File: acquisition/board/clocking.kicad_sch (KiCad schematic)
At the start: 58 parts, among them U11 LMK04806, U12 SIT9002AC-232N33EO100.00000, U14 74AVCH1T45, U15 74AVCH1T45, U16 74AVCH1T45, U17 74AVCH1T45, U19 74AVCH1T45, U20 74AVCH1T45

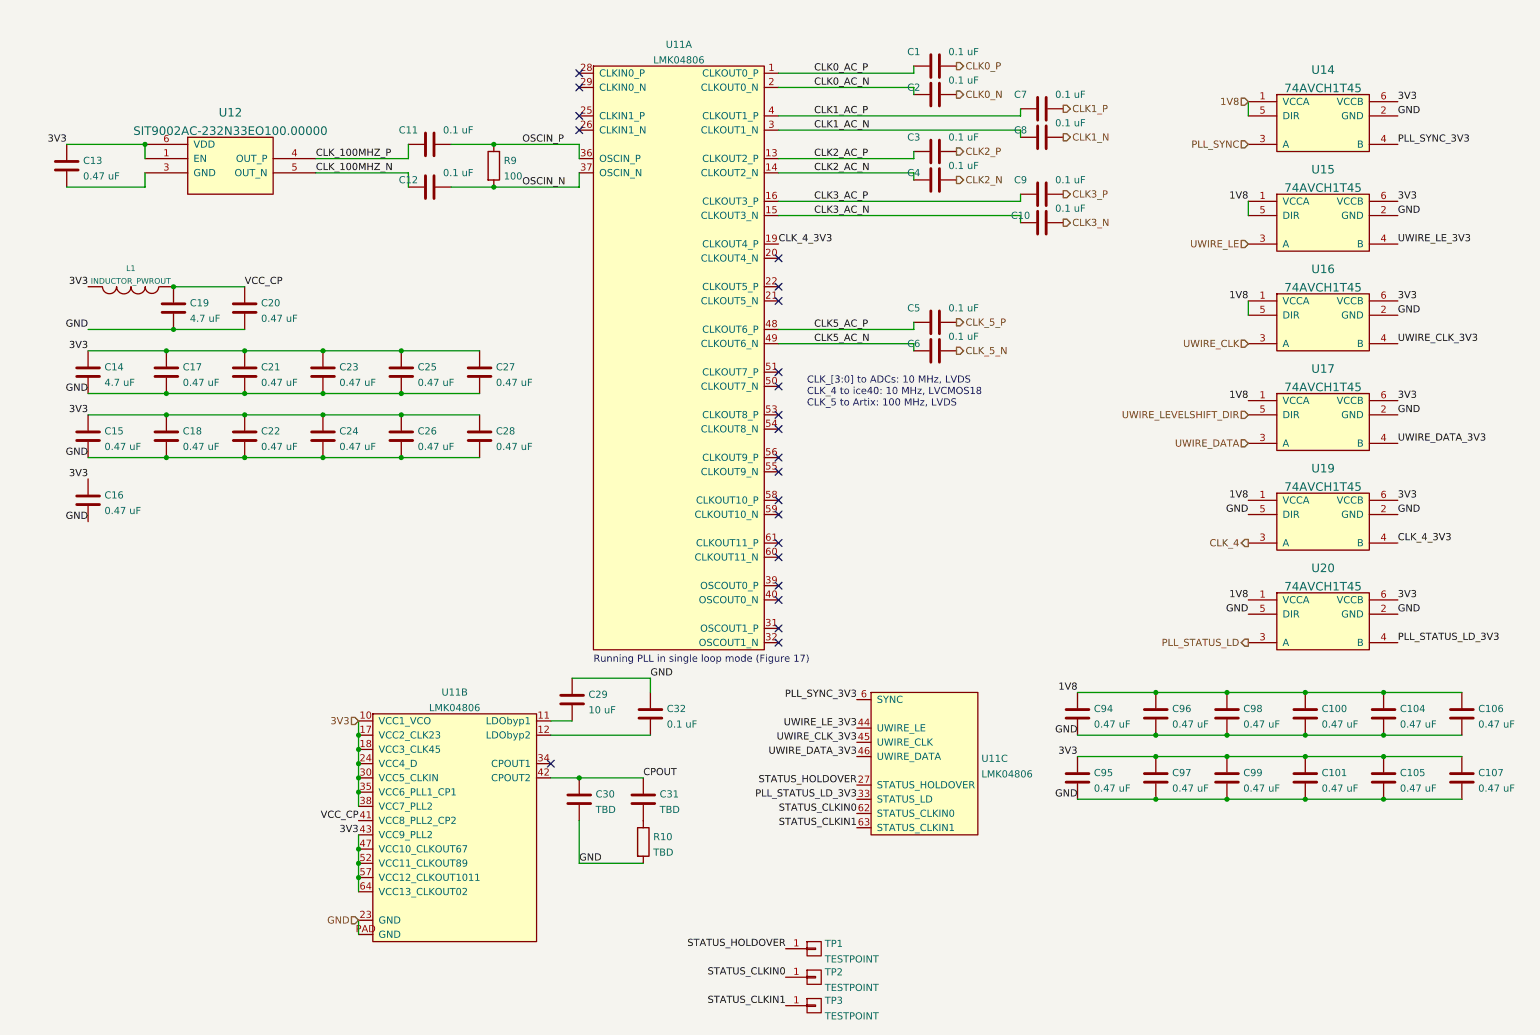
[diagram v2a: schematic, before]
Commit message: Lots of progress on power supply design, added a bunch of test points, etc
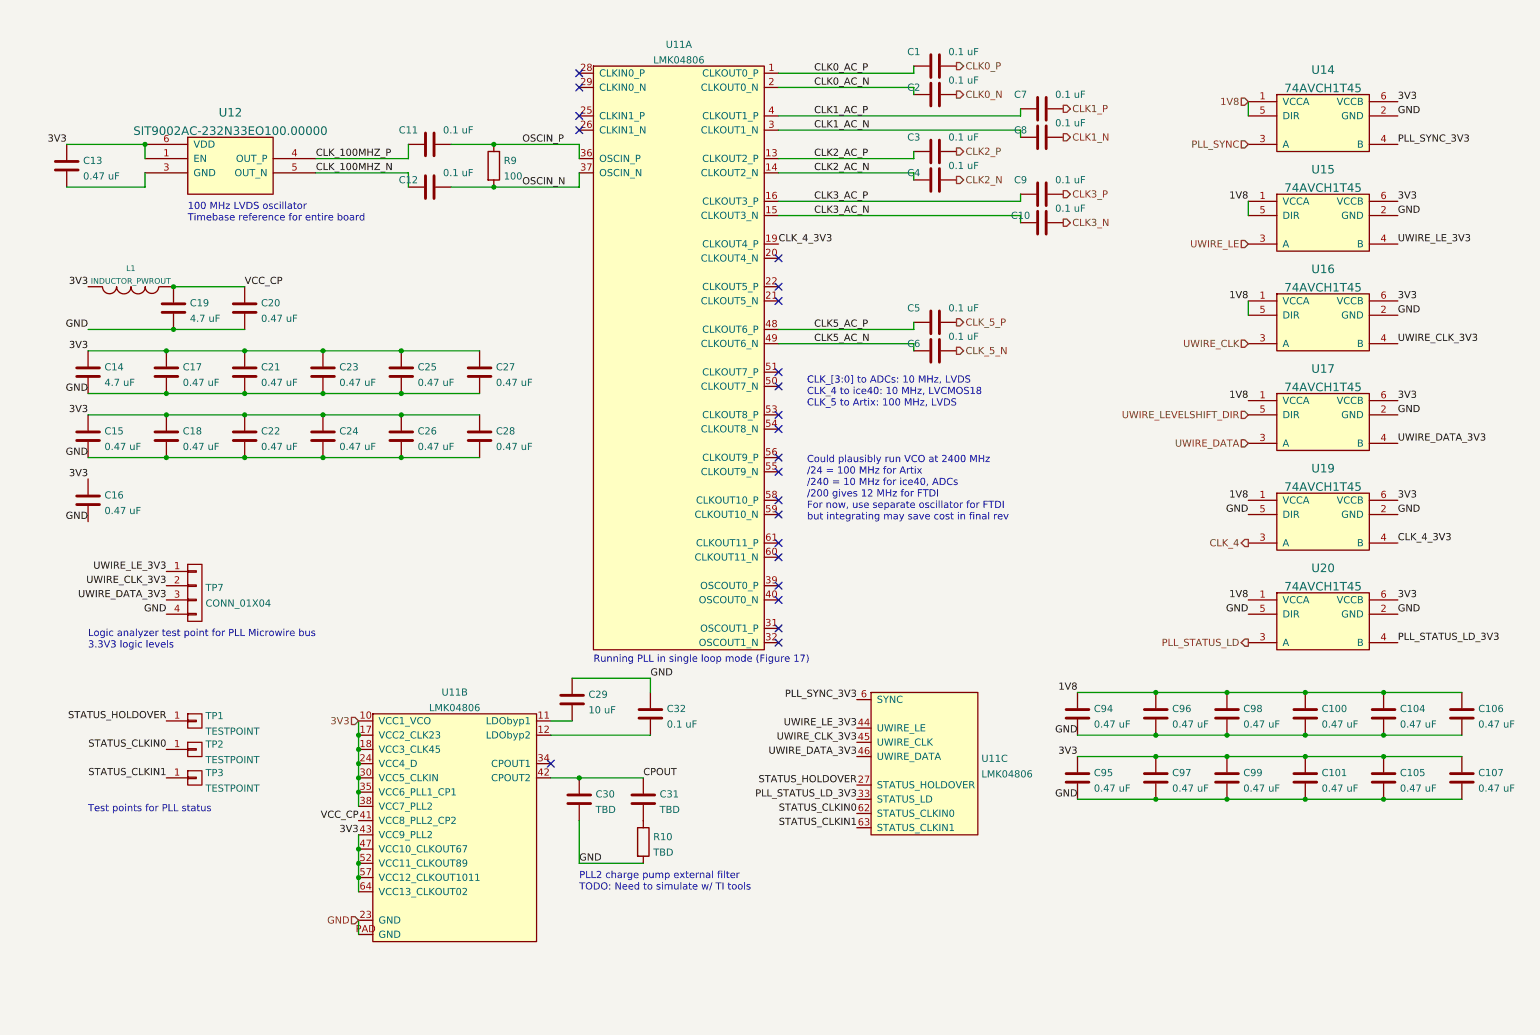
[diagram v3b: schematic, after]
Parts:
- added TP7: CONN_01X04, symbol conn:CONN_01X04
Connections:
- net GND: now also TP7.4 (P4)
- net UWIRE_CLK_3V3: now also TP7.2 (P2)
- net UWIRE_DATA_3V3: now also TP7.3 (P3)
- net UWIRE_LE_3V3: now also TP7.1 (P1)
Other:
- note added: "100 MHz LVDS oscillator Timebase reference for entire board"
- note added: "Could plausibly run VCO at 2400 MHz /24 = 100 MHz for Artix /240 = 10 MHz for ice40, ADCs /200 gives 12 MHz for FTDI For now, use separate oscillator for FTDI but integrating may save cost in final rev"
- note added: "Logic analyzer test point for PLL Microwire bus 3.3V3 logic levels"
- note added: "PLL2 charge pump external filter TODO: Need to simulate w/ TI tools"
- note added: "Test points for PLL status"
- moved on the sheet: TP1, TP2, TP3
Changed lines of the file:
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@@
   (title_block
     (title "Digitizer board")
-    (date "2022-07-04")
+    (date "2022-07-05")
     (rev "0.1")
     (company "A. Zonenberg")
@@
     (stroke (width 0) (type default) (color 0 0 0 0))
   )
+  (text "100 MHz LVDS oscillator\nTimebase reference for entire board"
+    (at 43.18 52.07 0)
+    (effects (font (size 1.27 1.27)) (justify left bottom))
+  )
+  (text "Test points for PLL status" (at 25.4 157.48 0)
+    (effects (font (size 1.27 1.27)) (justify left bottom))
+  )
   (text "CLK_[3:0] to ADCs: 10 MHz, LVDS\nCLK_4 to ice40: 10 MHz, LVCMOS18\nCLK_5 to Artix: 100 MHz, LVDS"
     (at 153.67 85.09 0)
@@
     (effects (font (size 1.27 1.27)) (justify left bottom))
   )
+  (text "Could plausibly run VCO at 2400 MHz\n/24 = 100 MHz for Artix\n/240 = 10 MHz for ice40, ADCs\n/200 gives 12 MHz for FTDI\nFor now, use separate oscillator for FTDI\nbut integrating may save cost in final rev"
+    (at 153.67 105.41 0)
+    (effects (font (size 1.27 1.27)) (justify left bottom))
+  )
+  (text "Logic analyzer test point for PLL Microwire bus\n3.3V3 logic levels"
+    (at 25.4 128.27 0)
+    (effects (font (size 1.27 1.27)) (justify left bottom))
+  )
+  (text "PLL2 charge pump external filter\nTODO: Need to simulate w/ TI tools"
+    (at 113.03 171.45 0)
+    (effects (font (size 1.27 1.27)) (justify left bottom))
+  )
   (label "CLK_4_3V3" (at 259.08 109.22 0)
     (effects (font (size 1.27 1.27)) (justify left bottom))
@@
     (effects (font (size 1.27 1.27)) (justify left bottom))
   )
+  (label "UWIRE_DATA_3V3" (at 39.37 119.38 180)
+    (effects (font (size 1.27 1.27)) (justify right bottom))
+  )
   (label "GND" (at 201.93 143.51 180)
     (effects (font (size 1.27 1.27)) (justify right bottom))
@@
     (effects (font (size 1.27 1.27)) (justify right bottom))
   )
+  (label "UWIRE_LE_3V3" (at 39.37 114.3 180)
+    (effects (font (size 1.27 1.27)) (justify right bottom))
+  )
   (label "UWIRE_DATA_3V3" (at 259.08 91.44 0)
     (effects (font (size 1.27 1.27)) (justify left bottom))
@@
     (effects (font (size 1.27 1.27)) (justify right bottom))
   )
-  (label "STATUS_CLKIN0" (at 149.86 186.69 180)
+  (label "STATUS_CLKIN0" (at 39.37 146.05 180)
     (effects (font (size 1.27 1.27)) (justify right bottom))
   )
@@
     (effects (font (size 1.27 1.27)) (justify left bottom))
   )
+  (label "UWIRE_CLK_3V3" (at 39.37 116.84 180)
+    (effects (font (size 1.27 1.27)) (justify right bottom))
+  )
   (label "UWIRE_CLK_3V3" (at 259.08 73.66 0)
     (effects (font (size 1.27 1.27)) (justify left bottom))
@@
     (effects (font (size 1.27 1.27)) (justify left bottom))
   )
-  (label "STATUS_CLKIN1" (at 149.86 191.77 180)
+  (label "STATUS_CLKIN1" (at 39.37 151.13 180)
     (effects (font (size 1.27 1.27)) (justify right bottom))
   )
@@
     (effects (font (size 1.27 1.27)) (justify left bottom))
   )
-  (label "STATUS_HOLDOVER" (at 149.86 181.61 180)
+  (label "STATUS_HOLDOVER" (at 39.37 140.97 180)
     (effects (font (size 1.27 1.27)) (justify right bottom))
   )
@@
   )
   (label "3V3" (at 25.4 63.5 180)
+    (effects (font (size 1.27 1.27)) (justify right bottom))
+  )
+  (label "GND" (at 39.37 121.92 180)
     (effects (font (size 1.27 1.27)) (justify right bottom))
   )
@@
     (pin "1")
     (pin "2")
+  )
+  (symbol (lib_id "conn:CONN_01X04") (at 44.45 118.11 0) (unit 1)
+    (in_bom yes) (on_board yes) (fields_autoplaced)
+    (property "Reference" "TP7" (id 0) (at 46.355 117.2015 0)
+      (effects (font (size 1.27 1.27)) (justify left))
+    )
+    (property "Value" "CONN_01X04" (id 1) (at 46.355 119.9766 0)
+      (effects (font (size 1.27 1.27)) (justify left))
+    )
+    (property "Footprint" "" (id 2) (at 44.45 118.11 0)
+      (effects (font (size 1.27 1.27)) hide)
+    )
+    (property "Datasheet" "" (id 3) (at 44.45 118.11 0)
+      (effects (font (size 1.27 1.27)) hide)
+    )
+    (pin "1")
+    (pin "2")
+    (pin "3")
+    (pin "4")
   )
   (symbol (lib_id "device:C") (at 53.34 90.17 0) (mirror y) (unit 1)
@@
     (pin "6")
   )
-  (symbol (lib_id "conn:CONN_01X01") (at 154.94 191.77 0) (unit 1)
-    (in_bom yes) (on_board yes) (fields_autoplaced)
-    (property "Reference" "TP3" (id 0) (at 156.845 190.8615 0)
-      (effects (font (size 1.27 1.27)) (justify left))
-    )
-    (property "Value" "TESTPOINT" (id 1) (at 156.845 193.6366 0)
-      (effects (font (size 1.27 1.27)) (justify left))
-    )
-    (property "Footprint" "" (id 2) (at 154.94 191.77 0)
-      (effects (font (size 1.27 1.27)) hide)
-    )
-    (property "Datasheet" "" (id 3) (at 154.94 191.77 0)
+  (symbol (lib_id "conn:CONN_01X01") (at 44.45 151.13 0) (unit 1)
+    (in_bom yes) (on_board yes) (fields_autoplaced)
+    (property "Reference" "TP3" (id 0) (at 46.355 150.2215 0)
+      (effects (font (size 1.27 1.27)) (justify left))
+    )
+    (property "Value" "TESTPOINT" (id 1) (at 46.355 152.9966 0)
+      (effects (font (size 1.27 1.27)) (justify left))
+    )
+    (property "Footprint" "" (id 2) (at 44.45 151.13 0)
+      (effects (font (size 1.27 1.27)) hide)
+    )
+    (property "Datasheet" "" (id 3) (at 44.45 151.13 0)
       (effects (font (size 1.27 1.27)) hide)
     )
@@
     (pin "2")
   )
-  (symbol (lib_id "conn:CONN_01X01") (at 154.94 186.69 0) (unit 1)
-    (in_bom yes) (on_board yes) (fields_autoplaced)
-    (property "Reference" "TP2" (id 0) (at 156.845 185.7815 0)
-      (effects (font (size 1.27 1.27)) (justify left))
-    )
-    (property "Value" "TESTPOINT" (id 1) (at 156.845 188.5566 0)
-      (effects (font (size 1.27 1.27)) (justify left))
-    )
-    (property "Footprint" "" (id 2) (at 154.94 186.69 0)
-      (effects (font (size 1.27 1.27)) hide)
-    )
-    (property "Datasheet" "" (id 3) (at 154.94 186.69 0)
+  (symbol (lib_id "conn:CONN_01X01") (at 44.45 146.05 0) (unit 1)
+    (in_bom yes) (on_board yes) (fields_autoplaced)
+    (property "Reference" "TP2" (id 0) (at 46.355 145.1415 0)
+      (effects (font (size 1.27 1.27)) (justify left))
+    )
+    (property "Value" "TESTPOINT" (id 1) (at 46.355 147.9166 0)
+      (effects (font (size 1.27 1.27)) (justify left))
+    )
+    (property "Footprint" "" (id 2) (at 44.45 146.05 0)
+      (effects (font (size 1.27 1.27)) hide)
+    )
+    (property "Datasheet" "" (id 3) (at 44.45 146.05 0)
       (effects (font (size 1.27 1.27)) hide)
     )
@@
     (pin "2")
   )
-  (symbol (lib_id "conn:CONN_01X01") (at 154.94 181.61 0) (unit 1)
-    (in_bom yes) (on_board yes) (fields_autoplaced)
-    (property "Reference" "TP1" (id 0) (at 156.845 180.7015 0)
-      (effects (font (size 1.27 1.27)) (justify left))
-    )
-    (property "Value" "TESTPOINT" (id 1) (at 156.845 183.4766 0)
-      (effects (font (size 1.27 1.27)) (justify left))
-    )
-    (property "Footprint" "" (id 2) (at 154.94 181.61 0)
-      (effects (font (size 1.27 1.27)) hide)
-    )
-    (property "Datasheet" "" (id 3) (at 154.94 181.61 0)
-      (effects (font (size 1.27 1.27)) hide)
-    )
+  (symbol (lib_id "conn:CONN_01X01") (at 44.45 140.97 0) (unit 1)
+    (in_bom yes) (on_board yes) (fields_autoplaced)
+    (property "Reference" "TP1" (id 0) (at 46.355 140.0615 0)
+      (effects (font (size 1.27 1.27)) (justify left))
+    )
+    (property "Value" "TESTPOINT" (id 1) (at 46.355 142.8366 0)
+      (effects (font (size 1.27 1.27)) (justify left))
+    )
+    (property "Footprint" "" (id 2) (at 44.45 140.97 0)
+      (effects (font (size 1.27 1.27)) hide)
+    )
+    (property "Datasheet" "" (id 3) (at 44.45 140.97 0)
+      (effects (font (size 1.27 1.27)) hide)
+    )

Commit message: More power supply work, added PLL loop filter, soft start, began assigning footprints
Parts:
- C1, C10, C100, C101, C104, C105, C106, C107, C11, C12, C13, C15, C16, C17, C18, C2, C20, C21, C22, C23, C24, C25, C26, C27, C28, C3, C32, C4, C5, C6, C7, C8, C9, C94, C95, C96, C97, C98, C99: footprint (none) -> azonenberg_pcb:EIA_0402_CAP_NOSILK
- C14, C19: footprint (none) -> azonenberg_pcb:EIA_0603_CAP_NOSILK
- C30: value TBD -> 47 pF
- C31: value TBD -> 3900 pF
- L1: value INDUCTOR_PWROUT -> FERRITE
- R10: value TBD -> 470; footprint (none) -> azonenberg_pcb:EIA_0402_RES_NOSILK
- R9: footprint (none) -> azonenberg_pcb:EIA_0402_RES_NOSILK
- TP1, TP2, TP3: footprint (none) -> azonenberg_pcb:TESTPOINT_SMT_0.5MM
- TP7: footprint (none) -> azonenberg_pcb:CONN_HEADER_2.54MM_1x4
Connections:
- net GND: now also C13.2, U12.3 (GND)
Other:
- note added: "PLL2 charge pump external filter Internal components: C3 = 10 pF C4 = 10 pF R3 = 200 R4 = 200"
- note removed: "PLL2 charge pump external filter TODO: Need to simulate w/ TI tools"

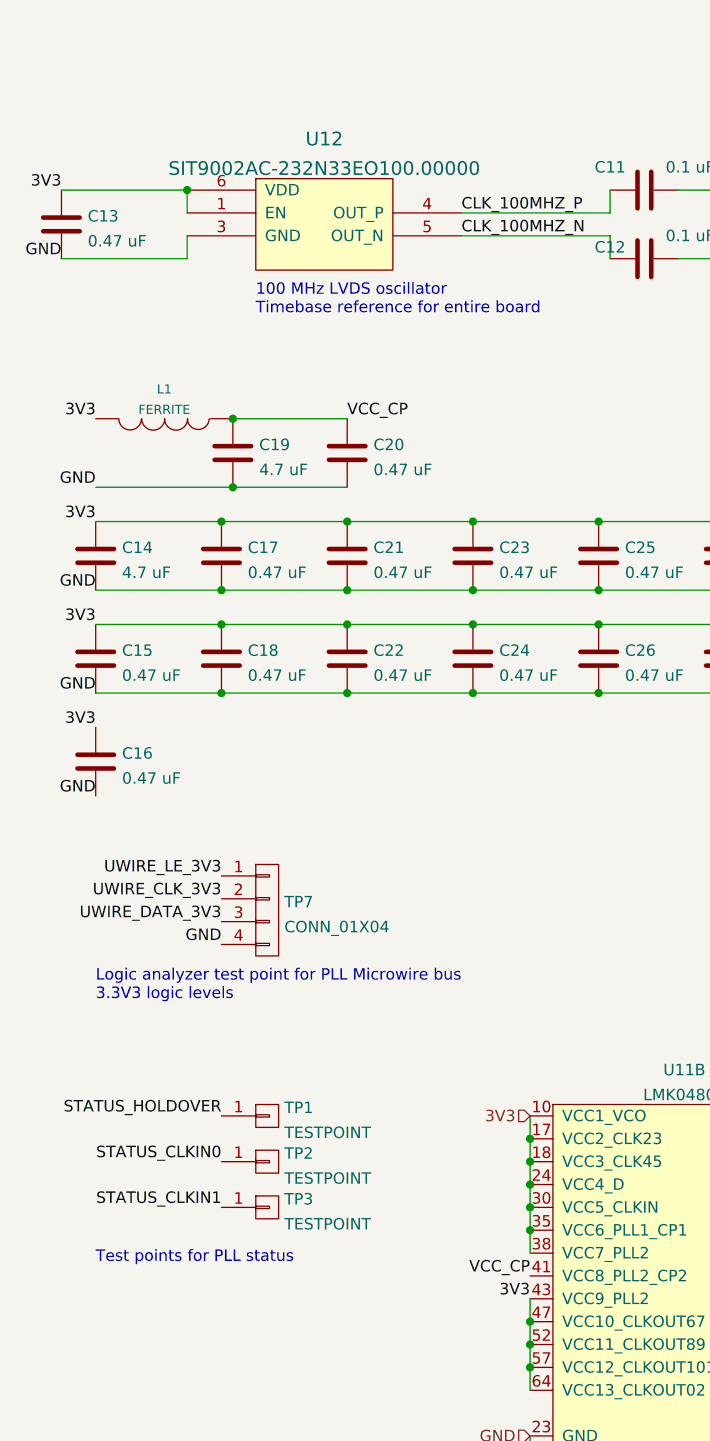
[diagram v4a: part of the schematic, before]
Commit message: Completed schematic after design review, ready for layout
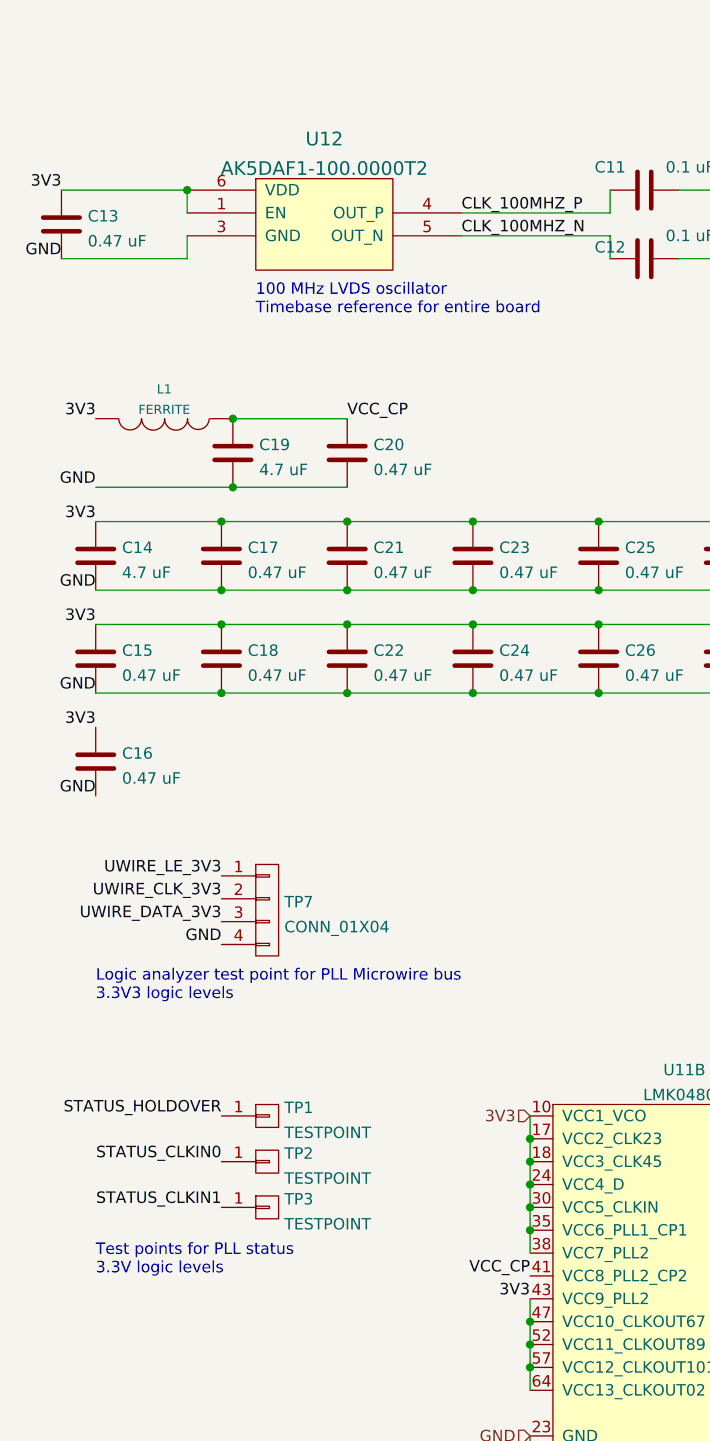
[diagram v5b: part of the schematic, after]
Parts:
- C29: footprint (none) -> azonenberg_pcb:EIA_0805_CAP_NOSILK
- C30, C31: footprint (none) -> azonenberg_pcb:EIA_0402_CAP_NOSILK
- U12: value SIT9002AC-232N33EO100.00000 -> AK5DAF1-100.0000T2
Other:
- note added: "Test points for PLL status 3.3V logic levels"
- note removed: "Test points for PLL status"
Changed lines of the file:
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@@
   (title_block
     (title "Digitizer board")
-    (date "2022-07-08")
+    (date "2022-07-17")
     (rev "0.1")
     (company "A. Zonenberg")
@@
     (effects (font (size 1.27 1.27)) (justify left bottom))
   )
-  (text "Test points for PLL status" (at 25.4 157.48 0)
+  (text "Test points for PLL status\n3.3V logic levels" (at 25.4 158.75 0)
     (effects (font (size 1.27 1.27)) (justify left bottom))
   )
@@
       (effects (font (size 1.27 1.27)) (justify left))
     )
-    (property "Footprint" "" (id 2) (at 112.7252 140.97 0)
+    (property "Footprint" "azonenberg_pcb:EIA_0805_CAP_NOSILK" (id 2) (at 112.7252 140.97 0)
       (effects (font (size 1.27 1.27)) hide)
     )
@@
       (effects (font (size 1.27 1.27)) (justify left))
     )
-    (property "Footprint" "" (id 2) (at 125.4252 158.75 0)
+    (property "Footprint" "azonenberg_pcb:EIA_0402_CAP_NOSILK" (id 2) (at 125.4252 158.75 0)
       (effects (font (size 1.27 1.27)) hide)
     )
@@
       (effects (font (size 1.524 1.524)))
     )
-    (property "Value" "SIT9002AC-232N33EO100.00000" (id 1) (at 50.8 35.7051 0)
+    (property "Value" "AK5DAF1-100.0000T2" (id 1) (at 50.8 35.7051 0)
       (effects (font (size 1.524 1.524)))
     )
@@
       (effects (font (size 1.27 1.27)) (justify left))
     )
-    (property "Footprint" "" (id 2) (at 113.9952 158.75 0)
-      (effects (font (size 1.27 1.27)) hide)
-    )
+    (property "Footprint" "azonenberg_pcb:EIA_0402_CAP_NOSILK" (id 2) (at 113.9952 158.75 0)
+      (effects (font (size 1.27 1.27)) hide)
+    )
